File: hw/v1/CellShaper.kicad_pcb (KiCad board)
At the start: 4 copper layers, 100 x 100 mm, 262 parts, among them J1 USB_C_Receptacle, J2 Screw_Terminal, J3 Conn_01x02, J4 USB_B_Micro, J5 SWD connector, J6 Conn_01x03, J7 Conn_01x03, Q1 ZVN4206G, Q10 ZVN4206G, Q11 IRFZ24NPbF, Q12 IRFZ24NPbF, Q13 ZVN4206G, Q14 ZVN4206G, Q15 Q_NMOS_GSD, Q2 IRFZ24NPbF, Q3 IRFZ24NPbF, Q4 ZVN4206G, Q5 IRFZ24NPbF, Q6 IRFZ24NPbF, Q7 ZVN4206G, Q8 IRFZ24NPbF, Q9 IRFZ24NPbF, U1 LMV344IPWR, U10 LP2985-3.3, U11 LP2985-5.0, U12 STM32F303RBTx, U13 DAC084S085, U2 MCP1416, U3 LMV344IPWR, U4 MCP1416, U5 LMV344IPWR, U6 MCP1416, U7 LMV344IPWR, U8 MCP1416, U9 FUSB302BMPX, Y1 8MHz crystal

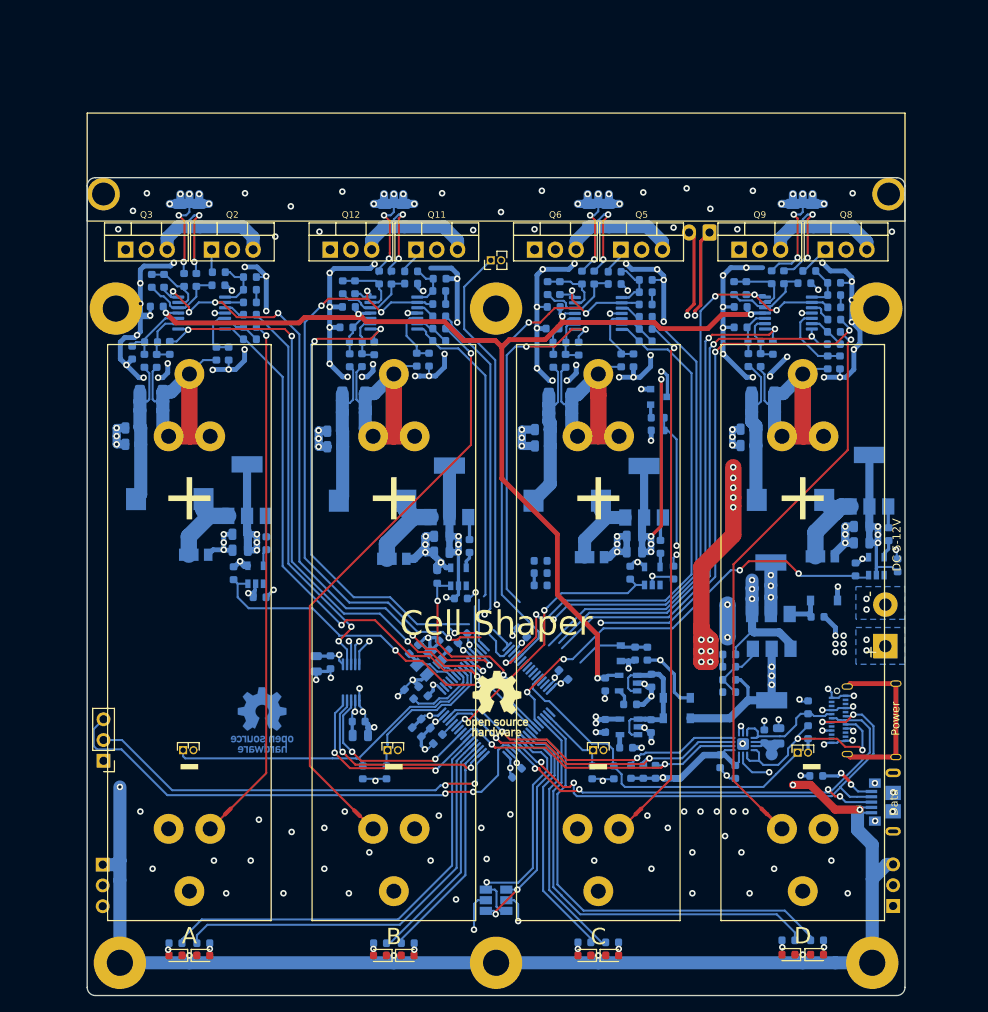
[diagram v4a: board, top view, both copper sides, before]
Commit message: Layout done and MCU pins rearranged
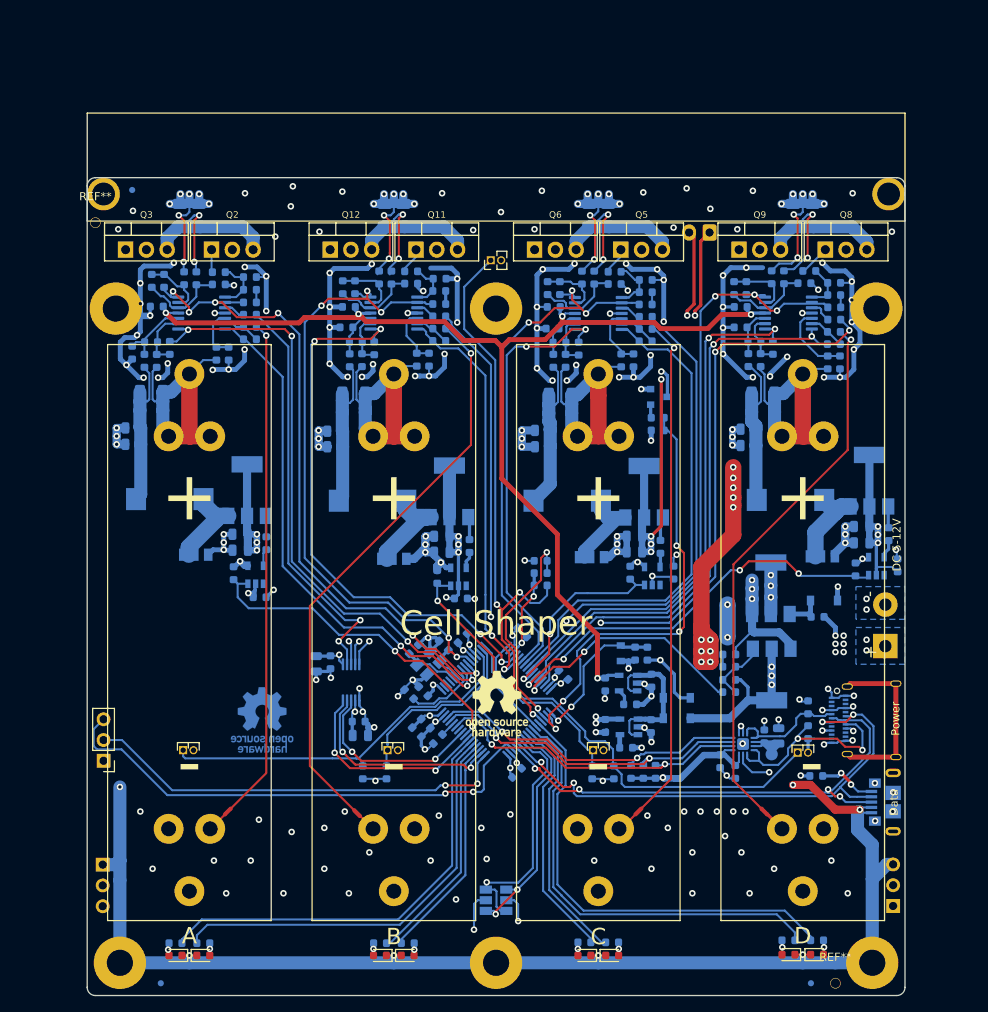
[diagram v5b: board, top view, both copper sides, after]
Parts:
- added REF**: MountingHole_2.1mm, MountingHole:MountingHole_2.1mm, F.Cu at (176.5, 143.5)
- added REF**: MountingHole_2.1mm, MountingHole:MountingHole_2.1mm, F.Cu at (86.0, 50.5)
- added REF**: Fiducial_0.75mm_Mask1.5mm, Fiducial:Fiducial_0.75mm_Mask1.5mm, B.Cu at (173.5, 143.5)
- added REF**: Fiducial_0.75mm_Mask1.5mm, Fiducial:Fiducial_0.75mm_Mask1.5mm, B.Cu at (94.0, 143.5)
- added REF**: Fiducial_0.75mm_Mask1.5mm, Fiducial:Fiducial_0.75mm_Mask1.5mm, B.Cu at (90.5, 46.5)
- Q1, Q10, Q4, Q7: value ZVN4206G -> ZVN4206GTA
- R112: value 27k -> 22k
- U12: value STM32F303RBTx -> STM32F303RDT6
- moved R18 0.20 mm to (98.3, 57.3)
- moved R21 0.20 mm to (96.8, 57.3)
- moved R17 0.11 mm to (101.1, 58.0)
- moved C12 0.10 mm to (140.7, 77.9)
- moved C13 0.10 mm to (140.7, 75.9)
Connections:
- U12 pad 10: /MCU/CELL_A_VOLTAGE -> /MCU/CELL_A_DISCHARGE_CURRENT
- U12 pad 11: /MCU/CELL_A_CHARGE_CURRENT -> /MCU/CELL_B_DISCHARGE_CURRENT
- U12 pad 14: /MCU/CELL_A_DISCHARGE_CURRENT -> /MCU/CELL_A_TEMPERATURE
- U12 pad 15: /MCU/PCB_TEMPERATURE -> /MCU/CELL_B_TEMPERATURE
- U12 pad 16: /MCU/HEATSINK_TEMPERATURE -> /MCU/CELL_C_TEMPERATURE
- U12 pad 17: /MCU/CELL_B_DISCHARGE_CURRENT -> /MCU/CELL_D_TEMPERATURE
- U12 pad 18: /MCU/CELL_B_CHARGE_CURRENT -> GND
- U12 pad 20: /MCU/CELL_C_VOLTAGE -> /MCU/CELL_B_CHARGE_CURRENT
- U12 pad 21: /MCU/CELL_C_DISCHARGE_CURRENT -> /MCU/CELL_B_VOLTAGE
- U12 pad 22: /MCU/CELL_C_CHARGE_CURRENT -> /MCU/CELL_C_DISCHARGE_CURRENT
- U12 pad 23: Net-(U12-Pad23) -> /MCU/CELL_C_CHARGE_CURRENT
- U12 pad 24: /MCU/CELL_D_CHARGE_CURRENT -> /MCU/CELL_C_VOLTAGE
- U12 pad 25: /MCU/CELL_D_VOLTAGE -> /MCU/CELL_D_CHARGE_CURRENT
- U12 pad 26: /MCU/CELL_D_DISCHARGE_CURRENT -> /MCU/CELL_C_CHARGE
- U12 pad 27: Net-(U12-Pad27) -> /MCU/CELL_D_CHARGE
- U12 pad 28: /MCU/CELL_D_TEMPERATURE -> /MCU/CELL_D_DISCHARGE_CURRENT
- U12 pad 29: Net-(U12-Pad29) -> /MCU/EN_POWER
- U12 pad 30: Net-(U12-Pad30) -> /MCU/CELL_D_VOLTAGE
- U12 pad 33: Net-(U12-Pad33) -> /MCU/CHARGE_VOLTAGE
- U12 pad 34: /MCU/CELL_C_TEMPERATURE -> /MCU/EN_FAN
- U12 pad 35: /MCU/CELL_D_DISCHARGE_LED -> /MCU/PCB_TEMPERATURE
- U12 pad 36: /MCU/CELL_D_CHARGE_LED -> /MCU/HEATSINK_TEMPERATURE
- U12 pad 37: /MCU/CELL_D_CHARGE -> /MCU/CELL_D_DISCHARGE_LED
- U12 pad 39: /MCU/CELL_A_CHARGE -> /MCU/CELL_D_CHARGE_LED
- U12 pad 56: /MCU/I2C_~INT -> /MCU/CELL_A_CHARGE
- U12 pad 59: /MCU/CELL_C_CHARGE -> /MCU/I2C_~INT
- U12 pad 8: /MCU/CELL_A_TEMPERATURE -> /MCU/CELL_A_VOLTAGE
- U12 pad 9: /MCU/CELL_B_TEMPERATURE -> /MCU/CELL_A_CHARGE_CURRENT
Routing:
- net /MCU/EN_FAN: track 16.5 -> 54.8 mm, vias 1 -> 4
- net /MCU/EN_POWER: track 0.00 -> 30.2 mm, vias 0 -> 2
- net /MCU/PCB_TEMPERATURE: track 5.66 -> 26.9 mm, vias 0 -> 2
- net /MCU/HEATSINK_TEMPERATURE: track 51.1 -> 70.3 mm, vias 1 -> 3
- net /MCU/CELL_C_TEMPERATURE: track 9.30 -> 22.5 mm
- net /MCU/CELL_C_CHARGE_CURRENT: track 45.0 -> 54.7 mm
- net /MCU/CELL_C_CHARGE: track 33.7 -> 24.5 mm
- net /MCU/CHARGE_VOLTAGE: track 9.16 -> 18.3 mm, vias 0 -> 2
- net /MCU/CELL_B_VOLTAGE: track 41.9 -> 50.6 mm, vias 1 -> 2
- net /MCU/CELL_D_TEMPERATURE: track 42.5 -> 50.3 mm
- net +3V3: track 58.6 -> 66.3 mm, vias 13 -> 14
- net /MCU/CELL_A_CHARGE: track 46.5 -> 41.4 mm
- net /MCU/CELL_D_VOLTAGE: track 65.9 -> 70.9 mm
- net /MCU/CELL_D_DISCHARGE_CURRENT: track 61.8 -> 66.8 mm
- net /MCU/CELL_C_VOLTAGE: track 66.2 -> 61.3 mm, vias 2 -> 0
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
